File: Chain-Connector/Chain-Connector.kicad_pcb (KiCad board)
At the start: 2 copper layers, 24.1 x 21.6 mm, 11 parts, among them P1 USB_A, P2 CONN_01X06, U1 SN74HC157PWR

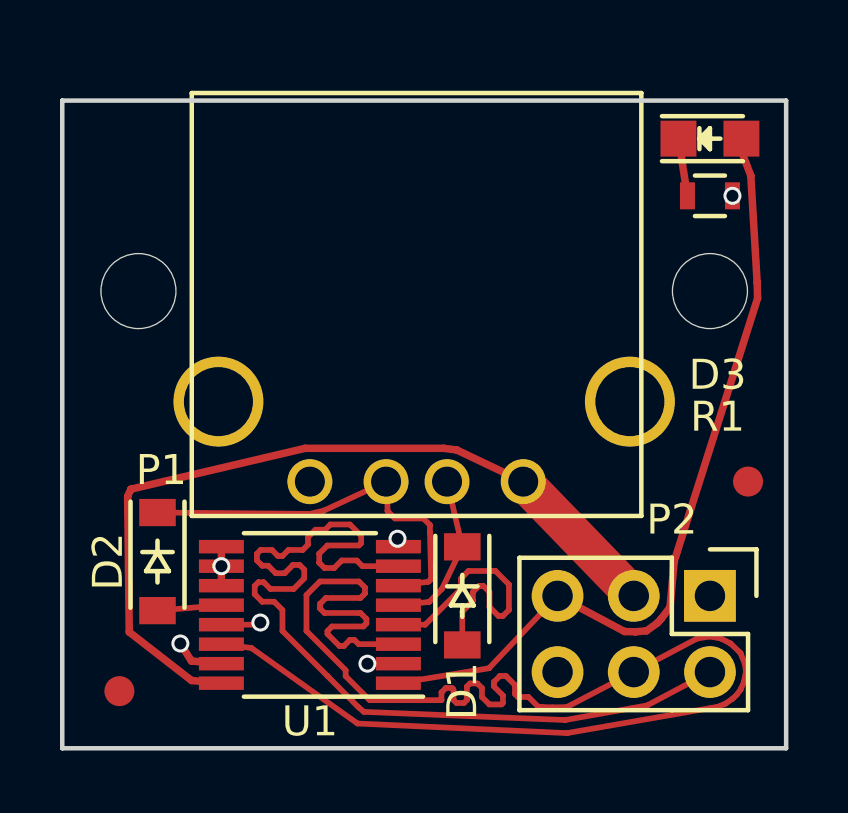
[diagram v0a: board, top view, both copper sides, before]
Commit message: Added the Option to use a Micro-USB Connector
And also revamped the Routing to be less of a Mess
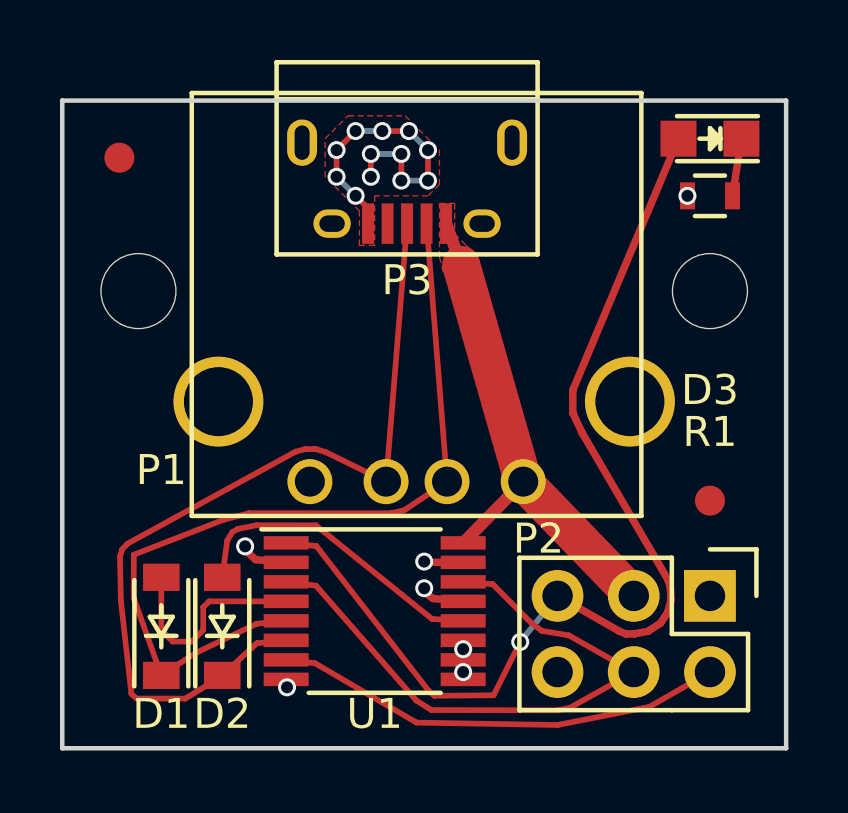
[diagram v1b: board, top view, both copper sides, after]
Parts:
- added P3: USB_OTG, Connect:USB_Micro-B, F.Cu at (148.7, 86.4)
- moved ? 17.8 mm to (139.1, 85.7)
- moved D1 10.1 mm to (140.5, 101.3), turned to 90 degrees
- moved D2 3.05 mm to (142.5, 101.3), turned to 90 degrees
- moved U1 2.16 mm to (147.6, 100.8), turned to 0 degrees
- moved ? 1.42 mm to (158.8, 97.2)
- turned D3 to 180 degrees
- turned R1 to 0 degrees
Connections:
- P2 pad 6: (no net) -> Net-(P2-Pad6)
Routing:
- net /TX0: track 51.0 -> 20.4 mm
- net /IO1: track 5.43 -> 28.4 mm
- net /RX0: track 31.5 -> 15.0 mm
- net /IO2: track 13.4 -> 29.3 mm
- net GND: track 5.79 -> 17.3 mm, vias 6 -> 19
- net VCC: track 27.3 -> 17.6 mm
- net Net-(D2-Pad2): track 2.14 -> 10.4 mm
- net /Master: track 26.9 -> 35.0 mm, vias 0 -> 1
- net Net-(D1-Pad2): track 9.79 -> 7.08 mm
- added copper zone on F.Cu, net GND
- added copper zone on F.Cu, net VCC
